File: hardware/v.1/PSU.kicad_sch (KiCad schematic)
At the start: 87 parts, among them J17 Barrel_Jack_Switch, J18 USB_C_Receptacle_USB2.0, Q5 2N7002, Q6 2N7002, Q7 NCE30P28Q, Q8 2N7002, SW1 SW_Push, SW2 SW_Push, U13 TL431DBZ, U14 CH224K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

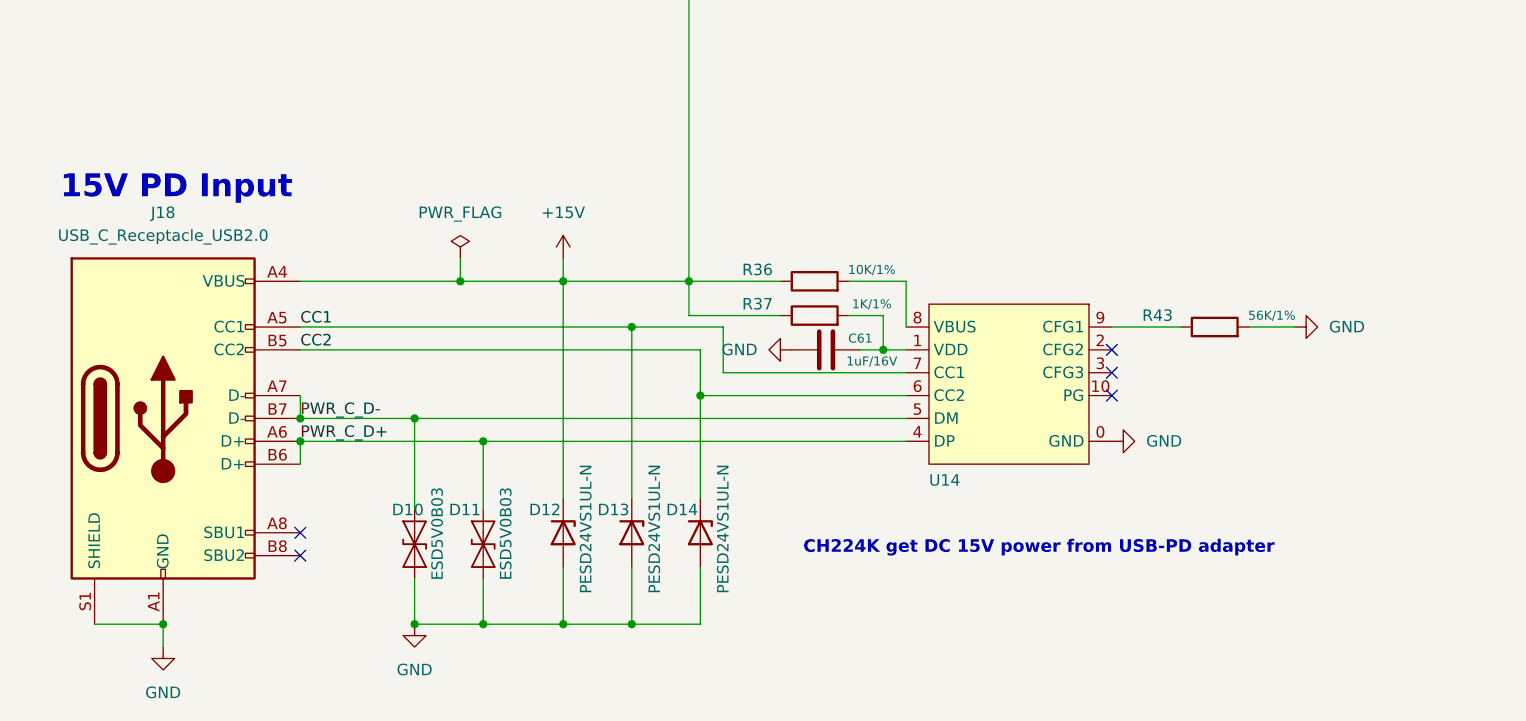
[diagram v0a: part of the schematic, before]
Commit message: pretty much finish the board, did bios chip, gpio, 4x sata
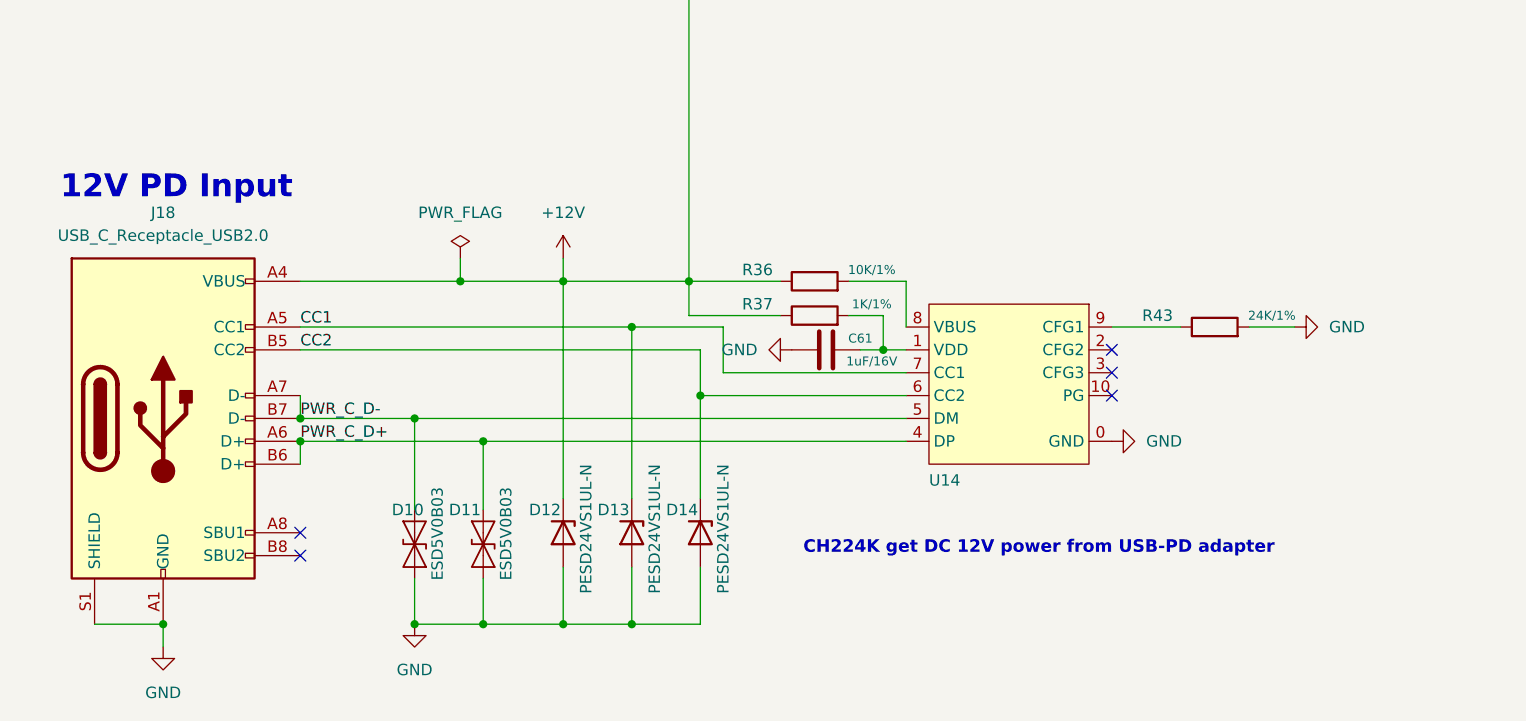
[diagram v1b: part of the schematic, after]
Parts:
- R43: value 56K/1% -> 24K/1%
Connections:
- net +15V is gone; now on net +12V: D12.1 (K), D18.2 (A), D19.2 (A), D20.2 (A), J18.A4 (VBUS), J18.A9 (VBUS), J18.B4 (VBUS), J18.B9 (VBUS), R36.1, R37.1, TP3.1
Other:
- note added: "12V PD Input"
- note added: "CH224K get DC 12V power from USB-PD adapter"
- note removed: "15V PD Input"
- note removed: "CH224K get DC 15V power from USB-PD adapter"
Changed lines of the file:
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@@
 		)
 	)
-	(text "15V PD Input"
+	(text "12V PD Input"
 		(exclude_from_sim no)
 		(at 162.56 237.49 0)
@@
 		)
 	)
-	(text "CH224K get DC 15V power from USB-PD adapter"
+	(text "CH224K get DC 12V power from USB-PD adapter"
 		(exclude_from_sim no)
 		(at 245.11 276.86 0)
@@
 			)
 		)
-		(property "Value" "56K/1%"
+		(property "Value" "24K/1%"
 			(at 297.18 250.19 90)
 			(effects
@@
 			)
 		)
-		(property "Value" "+15V"
+		(property "Value" "+12V"
 			(at 218.44 238.76 0)
 			(effects

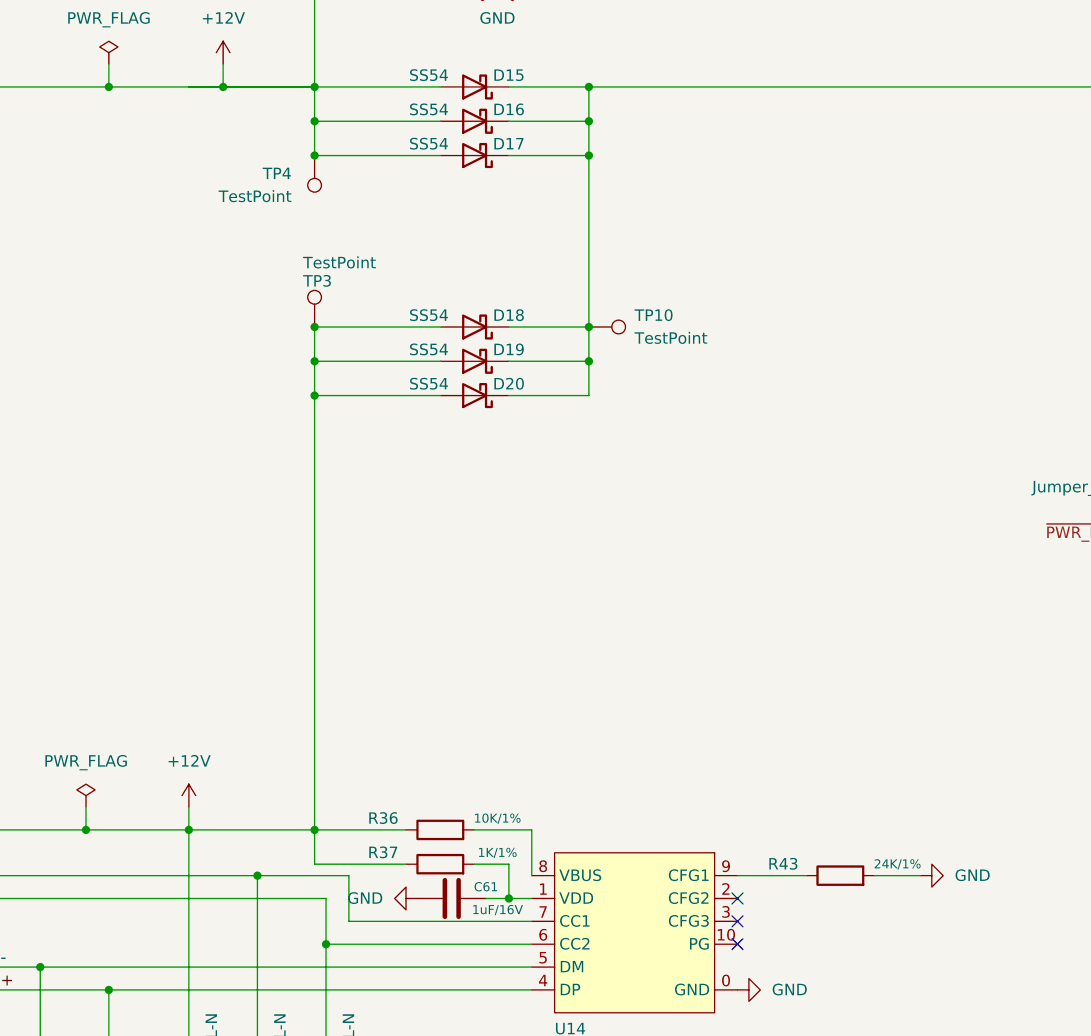
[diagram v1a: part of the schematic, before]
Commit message: design review finished: 0.4/0.2 vias changed to 0.4/0.3, VDC polygon and associated reroute, SATA connector, more ground vias, UART testpoints added, fixed unconnects; DRC at minimum. The BIOS sheet is faulty here (causing all remaining DRC errors)
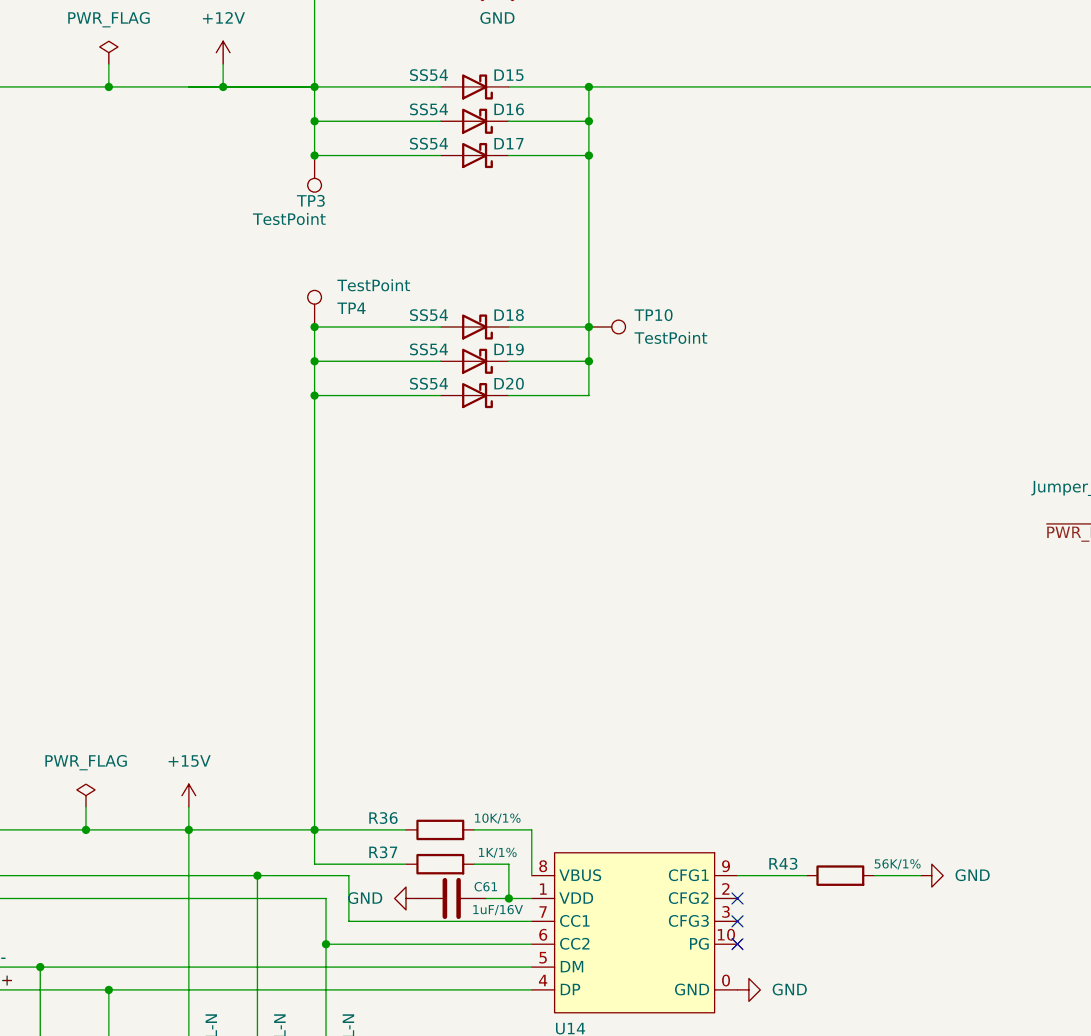
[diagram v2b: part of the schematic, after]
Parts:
- R43: value 24K/1% -> 56K/1%
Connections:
- net +12V: no longer D12.1 (K), D18.2 (A), D19.2 (A), D20.2 (A), J18.A4 (VBUS), J18.A9 (VBUS), J18.B4 (VBUS), J18.B9 (VBUS), R36.1, R37.1, TP4.1
- new net +15V: D12.1 (K), D18.2 (A), D19.2 (A), D20.2 (A), J18.A4 (VBUS), J18.A9 (VBUS), J18.B4 (VBUS), J18.B9 (VBUS), R36.1, R37.1, TP4.1
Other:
- moved on the sheet: TP3, TP4
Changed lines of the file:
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@@
 			"87qui6LwPM/Nr40xbgeRMcb9onCZCI04znmapkEQ5HnupghhGGI8QKuBe/trrX3fdy9zt0f0Vsbx"
 			"xO29QwghtJrhSRyEEEIYDBBCCGEwQAghBBgMEEIIAQYDhBBCgMEAIYQQYDBACCEEAP8ENoNYlZMu"
-			"IXEAAAAASUVORK5CYII="
+			"IXEAAAAASUVORK5CYIIAAAAAAAAAAAAAAEC60kNUVgAAGAAAAAAAAAAYAAAAAAAAABEAAAAAAAAA"
+			"MKbXQFRWAAAYAAAAAAAAABgAAAAAAAAAAAAAAAAAAABgptdAVFYAABsAAAAAAAAAGwAAAAAAAAAA"
+			"AAAAAAAAAJCm10BUVgAAGwAAAAAAAAAbAAAAAAAAAABvbGQAAAAAkF6aRFRWAAAbAAAAAAAAABsA"
+			"AAAAAAAAEQAAAAAAAADAXppEVFYAAB0AAAAAAAAAHQAAAAAAAAAAAAAAAAAAAPBemkRUVgAAGwAA"
+			"AAAAAAAbAAAAAAAAAG0AAAAAAAAAAPbvQVRWAAAcAAAAAAAAABwAAAAAAAAAHQAAAAAAAAAw9u9B"
+			"VFYAABwAAAAAAAAAHAAAAAAAAAAAAAAAAAAAAHCwP0VUVgAAFgAAAAAAAAAWAAAAAAAAANin/UJU"
+			"VgAAIF4zQVRWAAAXAAAAAAAAABcAAAAAAAAA+Kf9QlRWAABAg/9BVFYAABcAAAAAAAAAFwAAAAAA"
+			"AABghzFBVFYAAGD270FUVgAAGgAAAAAAAAAaAAAAAAAAAAAAAAAAAAAAgEATQVRWAAAaAAAAAAAA"
+			"ABoAAAAAAAAAAAAAAAAAAACwQBNBVFYAABoAAAAAAAAAGgAAAAAAAAAAAAAAAAAAAOBAE0FUVgAA"
+			"HAAAAAAAAAAcAAAAAAAAABEAAAAAAAAAgKJGQ1RWAAAaAAAAAAAAABoAAAAAAAAAAAAAAAAAAACw"
+			"okZDVFYAABsAAAAAAAAAGwAAAAAAAAAAAAAAAAAAAOCiRkNUVgAAGwAAAAAAAAAbAAAAAAAAAABv"
+			"bGQAVgAAgIL7QlRWAAAXAAAAAAAAABcAAAAAAAAAEQAAAAAAAAAgSPtBVFYAABQAAAAAAAAAFAAA"
+			"AAAAAAAAAAAAAAAAAEBI+0FUVgAAGQAAAAAAAAAZAAAAAAAAAJABAAAAAAAAcEj7QVRWAAAfAAAA"
+			"AAAAAB8AAAAAAAAAAAAAAAAAAADwsEpEVFYAACMAAAAAAAAAIwAAAAAAAABgpP1CVFYAACCxSkRU"
+			"VgAAJAAAAAAAAAAkAAAAAAAAALip/UJUVgAAULFKRFRWAAAfAAAAAAAAAB8AAAAAAAAA2Kn9QlRW"
+			"AAAQrwRAVFYAACAAAAAAAAAAIAAAAAAAAAAQHr1AVFYAAECvBEBUVgAAIgAAAAAAAAAiAAAAAAAA"
+			"AAAAAAAAAAAAcK8EQFRWAAAeAAAAAAAAAB4AAAAAAAAAAAAAAAAAAADwsXIZVFYAABUAAAAAAAAA"
+			"FQAAAAAAAAAAAAAAAAAAABCychlUVgAAEwAAAAAAAAATAAAAAAAAABEAAAAAAAAAMLJyGVRWAAAW"
+			"AAAAAAAAABYAAAAAAAAAAAAAAAAAAAAAAAAAAAAAAAAAAAAAAAAAAAAAAAAAAAAAAAAAAAAAAAAA"
+			"AAAAAAAAAAAAAAAAAAAAAAAAAAAAAAAAAAAAAAAAAAAAAAAAAAAAAAAAAAAAAAAAAAAAAAAAAAAA"
+			"AAAAAAAAAAAAAAAAAAAAAAAAAAAAAAAAAAAAAAAAAAAAAAAAAAAAAAAAAAAAAAAAAAAAAAAAAAAA"
+			"AAAAAAAAAAAAAAAAAAAAAAAAAAAAAAAAAAAAAAAAAAAAAAAAAAAAAAAAAAAAAAAAAAAAAAAAAAAA"
+			"AAAAAAAAAAAAAAAAAAAAAAAAAAAAAAAAAAAAAAAAAAAAAAAAAAAAAAAAAAAAAAAAAAAAAAAAAAAA"
+			"AAAAAAAAAAAAAAAAAAAAAAAAAAAAAAAAAAAAAAAAAAAAAAAAAAAAAAAAAAAAAAAAAAAAAAAAAAAA"
+			"AAAAAAAAAAAAAAAAAAAAAAAAAAAAAAAAAAAAAAAAAAAAAAAAAAAAAAAAAAAAAAAAAAAAAAAAAAAA"
+			"AAAAAAAAAAAAAAAAAAAAAAAAAAAAAAAAAAAAAAAAAAAAAAAAAAAAAAAAAAAAAAAAAAAAAAAAAAAA"
+			"AAAAAAAAAAAAAAAAAAAAAAAAAAAAAAAAAAAAAAAAAAAAAAAAAAAAAAAAAAAAAAAAAAAAAAAAAAAA"
+			"AAAAAAAAAAAAAAAAAAAAAAAAAAAAAAAAAAAAAAAAAAAAAAAAAAAAAAAAAAAAAAAAAAAAAAAAAAAA"
+			"AAAAAAAAAAAAAAAAAAAAAAAAAAAAAAAAAAAAAAAAAAAAAAAAAAAAAAAAAAAAAAAAAAAAAAAAAAAA"
+			"AAAAAAAAAAAAAAAAAAAAAAAAAAAAAAAAAAAAAAAAAAAAAAAAAAAAAAAAAAAAAAAAAAAAAAAAAAAA"
+			"AAAAAAAAAAAAAAAAAAAAAAAAAAAAAAAAAAAAAAAAAAAAAAAAAAAAAAAAAAAAAAAAAAAAAAAAAAAA"
+			"AAAAAAAAAAAAAAAAAAAAAAAAAAAAAAAAAAAAAAAAAAAAAAAAAAAAAAAAAAAAAAAAAAAAAAAAAAAA"
+			"AAAAAAAAAAAAAAAAAAAAAAAAAAAAAAAAAAAAAAAAAAAAAAAAAAAAAAAAAAAAAAAAAAAAAAAAAAAA"
+			"AAAAAAAAAAAAAAAAAAAAAAAAAAAAAAAAAAAAAAAAAAAAAAAAAAAAAAAAAAAAAAAAAAAAAAAAAAAA"
+			"AAAAAAAAAAAAAAAAAAAAAAAAAAAAAAAAAAAAAAAAAAAAAAAAAAAAAAAAAAAAAAAAAAAAAAAAAAAA"
+			"AAAAAAAAAAAAAAAAAAAAAAAAAAAAAAAAAAAAAAAAAAAAAAAAAAAAAAAAAAAAAAAAAAAAAAAAAAAA"
+			"AAAAAAAAAAAAAAAAAA=="
 		)
 	)
@@
 	(symbol
 		(lib_id "Connector:TestPoint")
-		(at 232.41 190.5 0)
+		(at 232.41 171.45 180)
 		(unit 1)
 		(exclude_from_sim no)
@@
 		(dnp no)
 		(property "Reference" "TP3"
-			(at 231.14 185.42 0)
+			(at 233.68 176.53 0)
 			(effects
 				(font
@@
 		)
 		(property "Value" "TestPoint"
-			(at 231.14 183.388 0)
+			(at 233.68 178.562 0)
 			(effects
 				(font
@@
 		)
 		(property "Footprint" "A_HDJ_Library:TestPoint_Pad_D1.5mm"
-			(at 237.49 190.5 0)
+			(at 227.33 171.45 0)
 			(effects
 				(font
@@
 		)
 		(property "Datasheet" "~"
-			(at 237.49 190.5 0)
+			(at 227.33 171.45 0)
 			(effects
 				(font
@@
 		)
 		(property "Description" "test point"
-			(at 232.41 190.5 0)
+			(at 232.41 171.45 0)
 			(effects
 				(font
@@
 		)
 		(property "Sim.Device" ""
-			(at 232.41 190.5 0)
+			(at 232.41 171.45 0)
 			(effects
 				(font
@@
 		)
 		(property "Sim.Pins" ""
-			(at 232.41 190.5 0)
+			(at 232.41 171.45 0)
 			(effects
 				(font
@@
 		)
 		(property "Sim.Type" ""
-			(at 232.41 190.5 0)
+			(at 232.41 171.45 0)
 			(effects
 				(font
@@
 	(symbol
 		(lib_id "Connector:TestPoint")
-		(at 232.41 171.45 0)
-		(mirror x)
+		(at 232.41 190.5 0)
+		(mirror y)
 		(unit 1)
 		(exclude_from_sim no)
@@
 		(fields_autoplaced yes)
 		(property "Reference" "TP4"
-			(at 229.87 173.4819 0)
+			(at 234.95 188.4681 0)
 			(effects
 				(font
@@
 		)
 		(property "Value" "TestPoint"
-			(at 229.87 176.0219 0)
+			(at 234.95 185.9281 0)
 			(effects
 				(font
@@
 		)
 		(property "Footprint" "A_HDJ_Library:TestPoint_Pad_D1.5mm"
-			(at 237.49 171.45 0)
+			(at 227.33 190.5 0)
 			(effects
 				(font
@@
 		)
 		(property "Datasheet" "~"
-			(at 237.49 171.45 0)
+			(at 227.33 190.5 0)
 			(effects
 				(font
@@
 		)
 		(property "Description" "test point"
-			(at 232.41 171.45 0)
+			(at 232.41 190.5 0)
 			(effects
 				(font
@@
 		)
 		(property "Sim.Device" ""
-			(at 232.41 171.45 0)
+			(at 232.41 190.5 0)
 			(effects
 				(font
@@
 		)
 		(property "Sim.Pins" ""
-			(at 232.41 171.45 0)
+			(at 232.41 190.5 0)
 			(effects
 				(font
@@
 		)
 		(property "Sim.Type" ""
-			(at 232.41 171.45 0)
+			(at 232.41 190.5 0)
 			(effects
 				(font
@@
 			)
 		)
-		(property "Value" "24K/1%"
+		(property "Value" "56K/1%"
 			(at 297.18 250.19 90)
 			(effects
@@
 			)
 		)
-		(property "Value" "+12V"
+		(property "Value" "+15V"
 			(at 218.44 238.76 0)
 			(effects

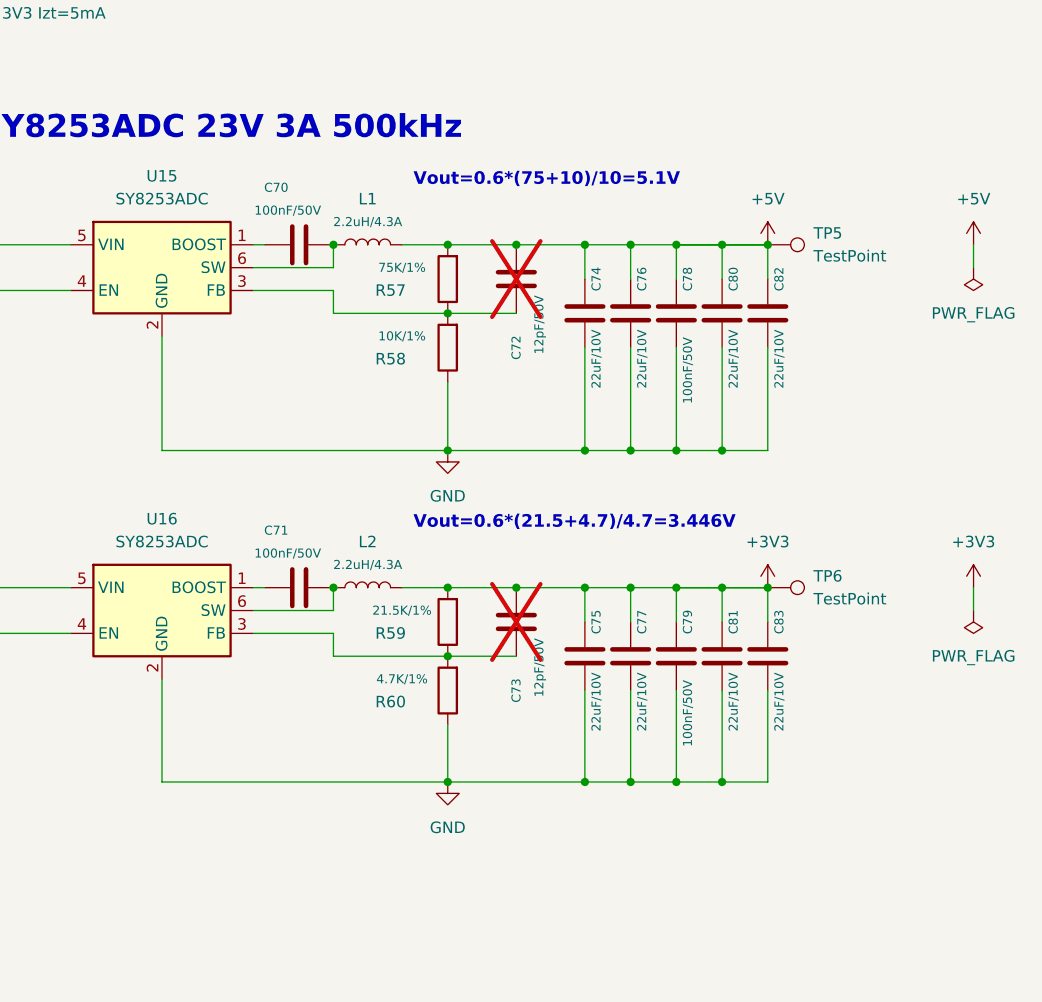
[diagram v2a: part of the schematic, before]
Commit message: remove some footprints to use digikey ones
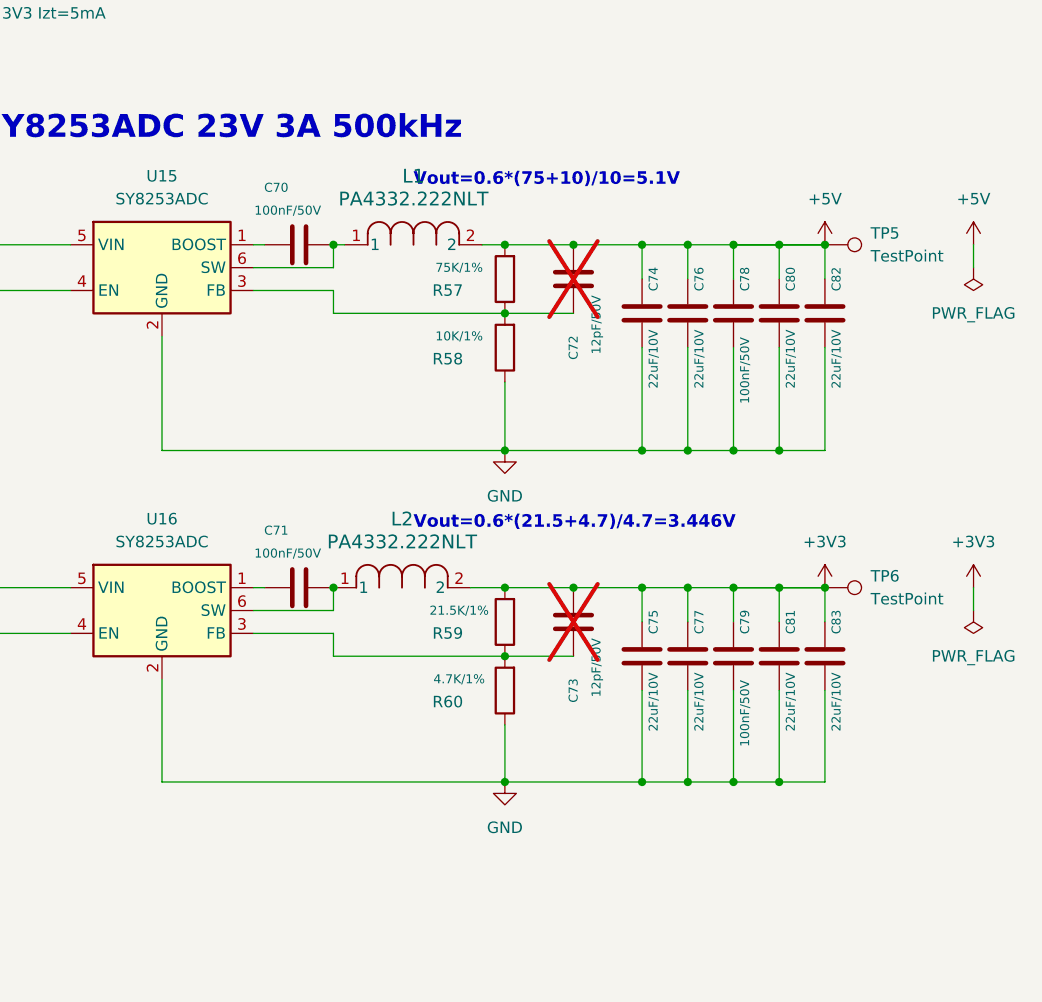
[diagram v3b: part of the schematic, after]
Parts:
- removed L1, L2: 2.2uH/4.3A, A_HDJ_Library:L_Sunlord_SWPA4020S, symbol Device:L
- added L1, L2: PA4332.222NLT, A_HDJ_Library:IND_PA4332.222NLT_PUL, symbol 2025-07-31_20-59-28:PA4332.222NLT
- J18: footprint A_HDJ_Library:USB_C_Receptacle_G-Switch_GT-USB-7010ASV -> Connector_USB:USB_C_Receptacle_JAE_DX07S016JA1R1500
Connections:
- net +3V3: now also L2.2
- net +5V: now also L1.2
- net at C71.1, U16.6 (SW): now also L2.1
- net at C70.1, U15.6 (SW): now also L1.1
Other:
- moved on the sheet: C72, C73, C74, C75, C76, C77, C78, C79, C80, C81, C82, C83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
